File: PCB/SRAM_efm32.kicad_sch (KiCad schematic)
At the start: 0 parts

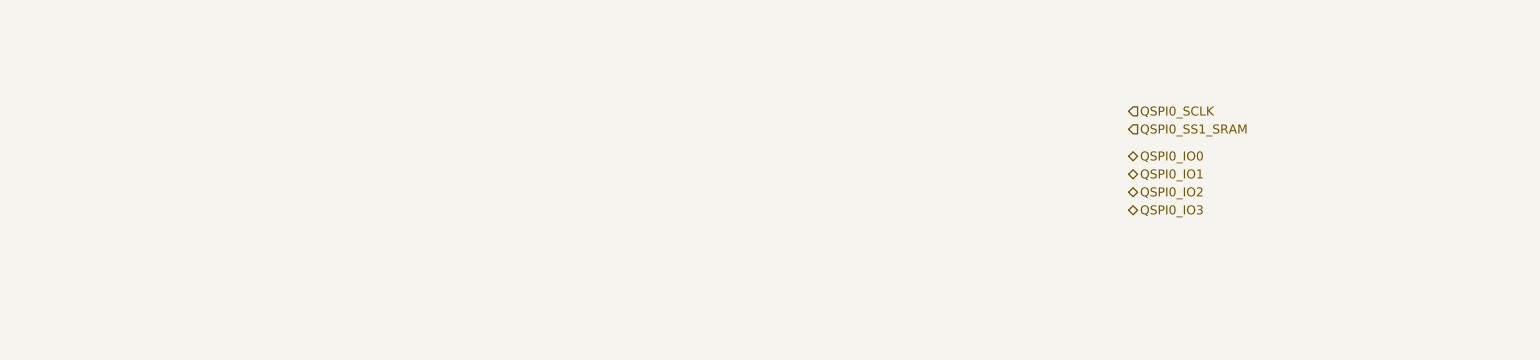
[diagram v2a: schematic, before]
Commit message: Attempt to set up SRAM
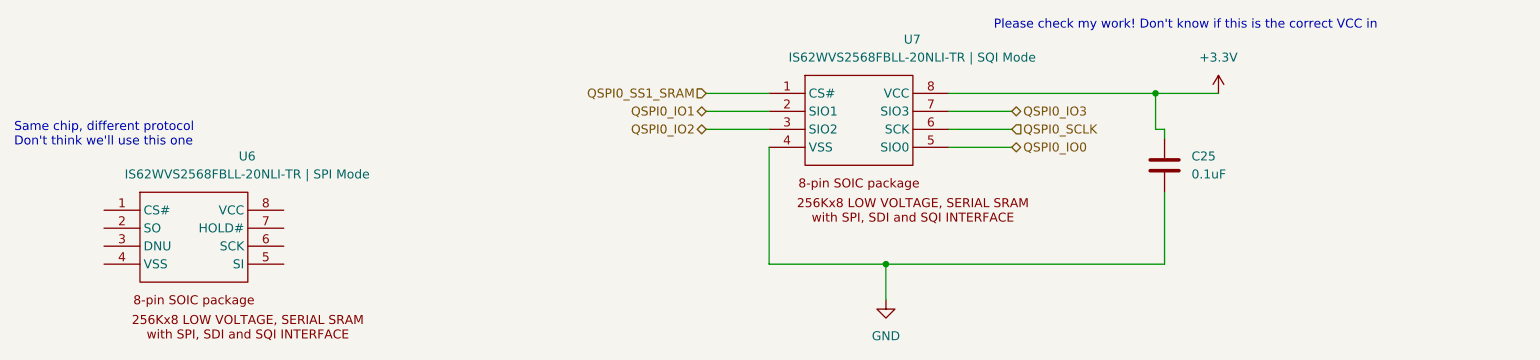
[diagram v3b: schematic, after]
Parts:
- added C25: 0.1uF, symbol Device:C
- added U6: IS62WVS2568FBLL-20NLI-TR | SPI Mode, symbol 0000_CustomComponents:IS62WVS2568FBLL-20NLI-TR | SPI Mode_1
- added U7: IS62WVS2568FBLL-20NLI-TR | SQI Mode, symbol 0000_CustomComponents:IS62WVS2568FBLL-20NLI-TR | SQI Mode
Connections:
- net QSPI0_IO0: now also U7.5 (SIO0)
- net QSPI0_IO1: now also U7.2 (SIO1)
- net QSPI0_IO2: now also U7.3 (SIO2)
- net QSPI0_IO3: now also U7.7 (SIO3)
- net QSPI0_SCLK: now also U7.6 (SCK)
- net QSPI0_SS1_SRAM: now also U7.1 (CS#)
- new net +3.3V: C25.1, U7.8 (VCC)
- new net GND: C25.2, U7.4 (VSS)
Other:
- note added: "Please check my work! Don't know if this is the correct VCC in"
- note added: "Same chip, different protocol Don't think we'll use this one"
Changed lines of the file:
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@@
 (kicad_sch (version 20230121) (generator eeschema)
   (paper "A4")
-  (hierarchical_label "QSPI0_SS1_SRAM" (shape input) (at 199.39 81.28 0) (fields_autoplaced)
+  (junction (at 165.1 100.33) (diameter 0) (color 0 0 0 0)
+  )
+  (junction (at 203.2 76.2) (diameter 0) (color 0 0 0 0)
+  )
+  (wire (pts (xy 139.7 78.74) (xy 148.59 78.74))
+    (stroke (width 0) (type default))
+  )
+  (wire (pts (xy 139.7 81.28) (xy 148.59 81.28))
+    (stroke (width 0) (type default))
+  )
+  (wire (pts (xy 203.2 81.28) (xy 203.2 76.2))
+    (stroke (width 0) (type default))
+  )
+  (wire (pts (xy 148.59 83.82) (xy 148.59 100.33))
+    (stroke (width 0) (type default))
+  )
+  (wire (pts (xy 182.88 78.74) (xy 173.99 78.74))
+    (stroke (width 0) (type default))
+  )
+  (wire (pts (xy 182.88 81.28) (xy 173.99 81.28))
+    (stroke (width 0) (type default))
+  )
+  (wire (pts (xy 173.99 76.2) (xy 203.2 76.2))
+    (stroke (width 0) (type default))
+  )
+  (wire (pts (xy 148.59 100.33) (xy 165.1 100.33))
+    (stroke (width 0) (type default))
+  )
+  (wire (pts (xy 204.47 81.28) (xy 203.2 81.28))
+    (stroke (width 0) (type default))
+  )
+  (wire (pts (xy 204.47 90.17) (xy 204.47 100.33))
+    (stroke (width 0) (type default))
+  )
+  (wire (pts (xy 204.47 81.28) (xy 204.47 82.55))
+    (stroke (width 0) (type default))
+  )
+  (wire (pts (xy 182.88 83.82) (xy 173.99 83.82))
+    (stroke (width 0) (type default))
+  )
+  (wire (pts (xy 165.1 100.33) (xy 204.47 100.33))
+    (stroke (width 0) (type default))
+  )
+  (wire (pts (xy 139.7 76.2) (xy 148.59 76.2))
+    (stroke (width 0) (type default))
+  )
+  (wire (pts (xy 165.1 100.33) (xy 165.1 105.41))
+    (stroke (width 0) (type default))
+  )
+  (wire (pts (xy 203.2 76.2) (xy 212.09 76.2))
+    (stroke (width 0) (type default))
+  )
+  (text "Same chip, different protocol\nDon't think we'll use this one\n"
+    (at 41.91 83.82 0)
+    (effects (font (size 1.27 1.27)) (justify left bottom))
+  )
+  (text "Please check my work! Don't know if this is the correct VCC in\n"
+    (at 180.34 67.31 0)
+    (effects (font (size 1.27 1.27)) (justify left bottom))
+  )
+  (hierarchical_label "QSPI0_SS1_SRAM" (shape input) (at 139.7 76.2 180) (fields_autoplaced)
+    (effects (font (size 1.27 1.27)) (justify right))
+  )
+  (hierarchical_label "QSPI0_IO3" (shape bidirectional) (at 182.88 78.74 0) (fields_autoplaced)
     (effects (font (size 1.27 1.27)) (justify left))
   )
-  (hierarchical_label "QSPI0_IO3" (shape bidirectional) (at 199.39 92.71 0) (fields_autoplaced)
+  (hierarchical_label "QSPI0_IO2" (shape bidirectional) (at 139.7 81.28 180) (fields_autoplaced)
+    (effects (font (size 1.27 1.27)) (justify right))
+  )
+  (hierarchical_label "QSPI0_SCLK" (shape input) (at 182.88 81.28 0) (fields_autoplaced)
     (effects (font (size 1.27 1.27)) (justify left))
   )
-  (hierarchical_label "QSPI0_IO2" (shape bidirectional) (at 199.39 90.17 0) (fields_autoplaced)
+  (hierarchical_label "QSPI0_IO1" (shape bidirectional) (at 139.7 78.74 180) (fields_autoplaced)
+    (effects (font (size 1.27 1.27)) (justify right))
+  )
+  (hierarchical_label "QSPI0_IO0" (shape bidirectional) (at 182.88 83.82 0) (fields_autoplaced)
     (effects (font (size 1.27 1.27)) (justify left))
   )
-  (hierarchical_label "QSPI0_SCLK" (shape input) (at 199.39 78.74 0) (fields_autoplaced)
-    (effects (font (size 1.27 1.27)) (justify left))
-  )
-  (hierarchical_label "QSPI0_IO1" (shape bidirectional) (at 199.39 87.63 0) (fields_autoplaced)
-    (effects (font (size 1.27 1.27)) (justify left))
-  )
-  (hierarchical_label "QSPI0_IO0" (shape bidirectional) (at 199.39 85.09 0) (fields_autoplaced)
-    (effects (font (size 1.27 1.27)) (justify left))
+  (symbol (lib_id "power:GND") (at 165.1 105.41 0) (unit 1)
+    (in_bom yes) (on_board yes) (dnp no) (fields_autoplaced)
+    (property "Reference" "#PWR014" (at 165.1 111.76 0)
+      (effects (font (size 1.27 1.27)) hide)
+    )
+    (property "Value" "GND" (at 165.1 110.49 0)
+      (effects (font (size 1.27 1.27)))
+    )
+    (property "Footprint" "" (at 165.1 105.41 0)
+      (effects (font (size 1.27 1.27)) hide)
+    )
+    (property "Datasheet" "" (at 165.1 105.41 0)
+      (effects (font (size 1.27 1.27)) hide)
+    )
+    (pin "1")
+    (instances
+      (project "RayTracingPCB"
+        (path "/e9047d94-28be-4266-894b-6ee25ef088bd/5a7a2c0a-f09d-4b4f-9411-f51dd121457c/3d4f3bb6-8d8f-4b26-b7c8-e791b7e32814"
+          (reference "#PWR014") (unit 1)
+        )
+        (path "/e9047d94-28be-4266-894b-6ee25ef088bd/e35285fd-162a-4f7e-974b-e69dceb1cfdc"
+          (reference "#PWR023") (unit 1)
+        )
+      )
+    )
+  )
+  (symbol (lib_id "0000_CustomComponents:IS62WVS2568FBLL-20NLI-TR | SPI Mode_1") (at 67.31 88.9 0) (unit 1)
+    (in_bom yes) (on_board yes) (dnp no) (fields_autoplaced)
+    (property "Reference" "U6" (at 74.8393 85.09 0)
+      (effects (font (size 1.27 1.27)))
+    )
+    (property "Value" "IS62WVS2568FBLL-20NLI-TR | SPI Mode" (at 74.8393 87.63 0)
+      (effects (font (size 1.27 1.27)))
+    )
+    (property "Footprint" "" (at 67.31 88.9 0)
+      (effects (font (size 1.27 1.27)) hide)
+    )
+    (property "Datasheet" "https://www.issi.com/WW/pdf/IS62-65WVS2568FALL-BLL.pdf" (at 67.31 88.9 0)
+      (effects (font (size 1.27 1.27)) hide)
+    )
+    (pin "1")
+    (pin "2")
+    (pin "3")
+    (pin "4")
+    (pin "5")
+    (pin "6")
+    (pin "7")
+    (pin "8")
+    (instances
+      (project "RayTracingPCB"
+        (path "/e9047d94-28be-4266-894b-6ee25ef088bd/e35285fd-162a-4f7e-974b-e69dceb1cfdc"
+          (reference "U6") (unit 1)
+        )
+      )
+    )
+  )
+  (symbol (lib_id "Device:C") (at 204.47 86.36 0) (unit 1)
+    (in_bom yes) (on_board yes) (dnp no) (fields_autoplaced)
+    (property "Reference" "C25" (at 208.28 85.09 0)
+      (effects (font (size 1.27 1.27)) (justify left))
+    )
+    (property "Value" "0.1uF" (at 208.28 87.63 0)
+      (effects (font (size 1.27 1.27)) (justify left))
+    )
+    (property "Footprint" "" (at 205.4352 90.17 0)
+      (effects (font (size 1.27 1.27)) hide)
+    )
+    (property "Datasheet" "~" (at 204.47 86.36 0)
+      (effects (font (size 1.27 1.27)) hide)
+    )
+    (pin "1")
+    (pin "2")
+    (instances
+      (project "RayTracingPCB"
+        (path "/e9047d94-28be-4266-894b-6ee25ef088bd/f9a74965-bde5-47a2-9f66-243cb6fc0f53"
+          (reference "C25") (unit 1)
+        )
+        (path "/e9047d94-28be-4266-894b-6ee25ef088bd/e35285fd-162a-4f7e-974b-e69dceb1cfdc"
+          (reference "C27") (unit 1)
+        )
+      )
+    )
+  )
+  (symbol (lib_id "0000_CustomComponents:IS62WVS2568FBLL-20NLI-TR | SQI Mode") (at 161.29 72.39 0) (unit 1)
+    (in_bom yes) (on_board yes) (dnp no) (fields_autoplaced)
+    (property "Reference" "U7" (at 168.8193 68.58 0)
+      (effects (font (size 1.27 1.27)))
+    )
+    (property "Value" "IS62WVS2568FBLL-20NLI-TR | SQI Mode" (at 168.8193 71.12 0)
+      (effects (font (size 1.27 1.27)))
+    )
+    (property "Footprint" "" (at 161.29 72.39 0)
+      (effects (font (size 1.27 1.27)) hide)
+    )
+    (property "Datasheet" "https://www.issi.com/WW/pdf/IS62-65WVS2568FALL-BLL.pdf" (at 161.29 72.39 0)
+      (effects (font (size 1.27 1.27)) hide)
+    )
+    (pin "1")
+    (pin "2")
+    (pin "3")
+    (pin "4")
+    (pin "5")
+    (pin "6")
+    (pin "7")
+    (pin "8")
+    (instances
+      (project "RayTracingPCB"
+        (path "/e9047d94-28be-4266-894b-6ee25ef088bd/e35285fd-162a-4f7e-974b-e69dceb1cfdc"
+          (reference "U7") (unit 1)
+        )
+      )
+    )
+  )
+  (symbol (lib_id "power:+3.3V") (at 212.09 76.2 0) (unit 1)
+    (in_bom yes) (on_board yes) (dnp no) (fields_autoplaced)
+    (property "Reference" "#PWR017" (at 212.09 80.01 0)
+      (effects (font (size 1.27 1.27)) hide)
+    )
+    (property "Value" "+3.3V" (at 212.09 71.12 0)
+      (effects (font (size 1.27 1.27)))
+    )
+    (property "Footprint" "" (at 212.09 76.2 0)
+      (effects (font (size 1.27 1.27)) hide)
+    )
+    (property "Datasheet" "" (at 212.09 76.2 0)
+      (effects (font (size 1.27 1.27)) hide)
+    )
+    (pin "1")
+    (instances
+      (project "RayTracingPCB"
+        (path "/e9047d94-28be-4266-894b-6ee25ef088bd/f9a74965-bde5-47a2-9f66-243cb6fc0f53"
+          (reference "#PWR017") (unit 1)
+        )
+        (path "/e9047d94-28be-4266-894b-6ee25ef088bd/e35285fd-162a-4f7e-974b-e69dceb1cfdc"
+          (reference "#PWR022") (unit 1)
+        )
+      )
+    )
   )
 )

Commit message: pcb: cleanup mcu sram
Signed-off-by: Kolbjørn Austreng <kolbjorn.austreng@hotzen.io>
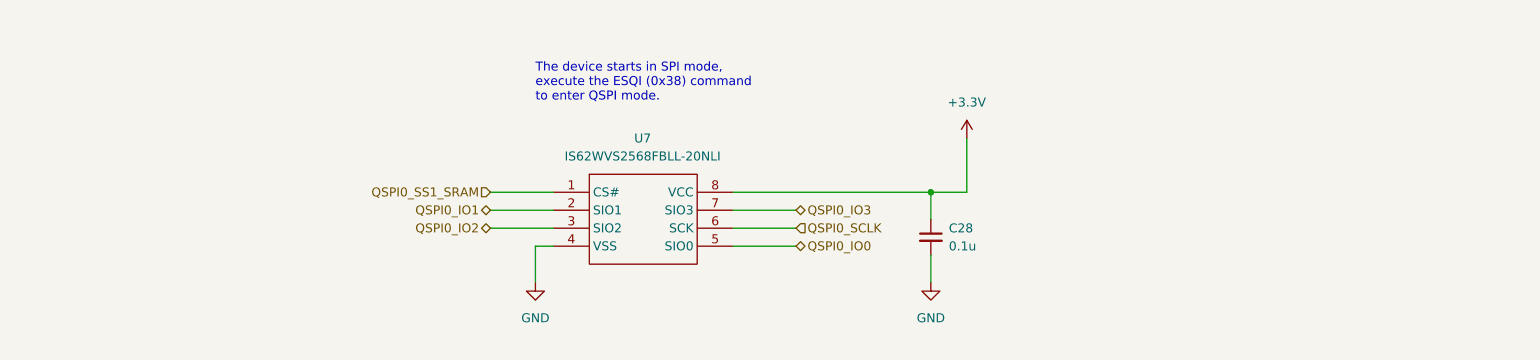
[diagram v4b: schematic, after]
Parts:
- removed C25: 0.1uF, symbol Device:C
- removed U6: IS62WVS2568FBLL-20NLI-TR | SPI Mode, symbol 0000_CustomComponents:IS62WVS2568FBLL-20NLI-TR | SPI Mode_1
- added C28: 0.1u, symbol Device:C_Small
- U7: value IS62WVS2568FBLL-20NLI-TR | SQI Mode -> IS62WVS2568FBLL-20NLI
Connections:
- net +3.3V: now also C28.1
- net GND: now also C28.2
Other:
- note added: "The device starts in SPI mode, execute the ESQI (0x38) command to enter QSPI mode."
- note removed: "Please check my work! Don't know if this is the correct VCC in"
- note removed: "Same chip, different protocol Don't think we'll use this one"
